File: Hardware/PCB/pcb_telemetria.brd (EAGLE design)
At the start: 77.5 x 104.1 mm, 33 parts

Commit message: update
adicao de rotas na pcb
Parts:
- moved SHUNTS 48.0 mm to (43.9, 3.87), turned to 0 degrees
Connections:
- net 25: no longer C_BAUX.2
- net 33: now also C_BAUX.2
- net C5: now also R20.1
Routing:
- net C5: track 0.00 -> 69.9 mm
- net C4: track 0.00 -> 69.6 mm
- net C7: track 0.49 -> 69.1 mm
- net C6: track 0.00 -> 68.3 mm
- net 2: track 9.94 -> 74.4 mm
- net 13: track 0.00 -> 46.1 mm
- net 33: track 0.00 -> 43.3 mm
- net C3: track 9.94 -> 32.6 mm
- net C2: track 24.6 -> 31.8 mm
- net C1: track 24.4 -> 30.9 mm
- net C0: track 25.3 -> 29.3 mm

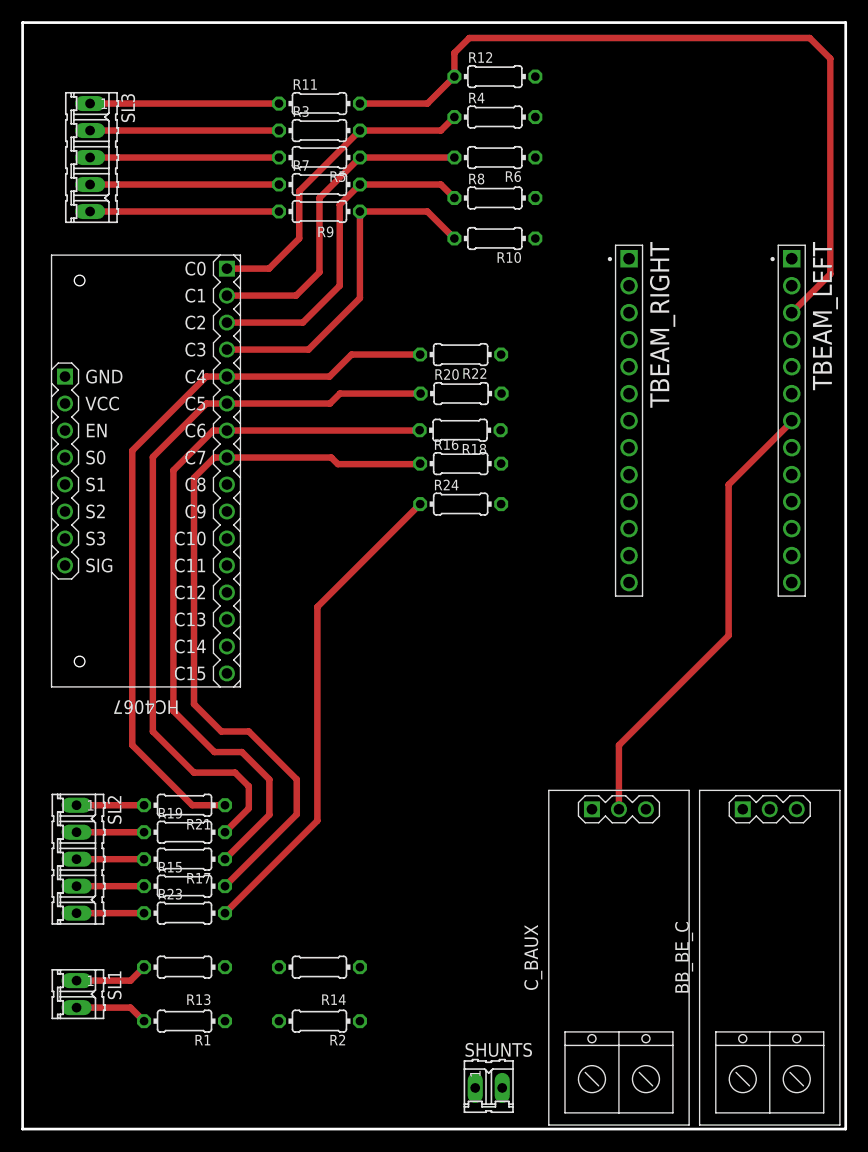
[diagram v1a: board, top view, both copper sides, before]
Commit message: Adicao de Rotas e mudanca de nomes
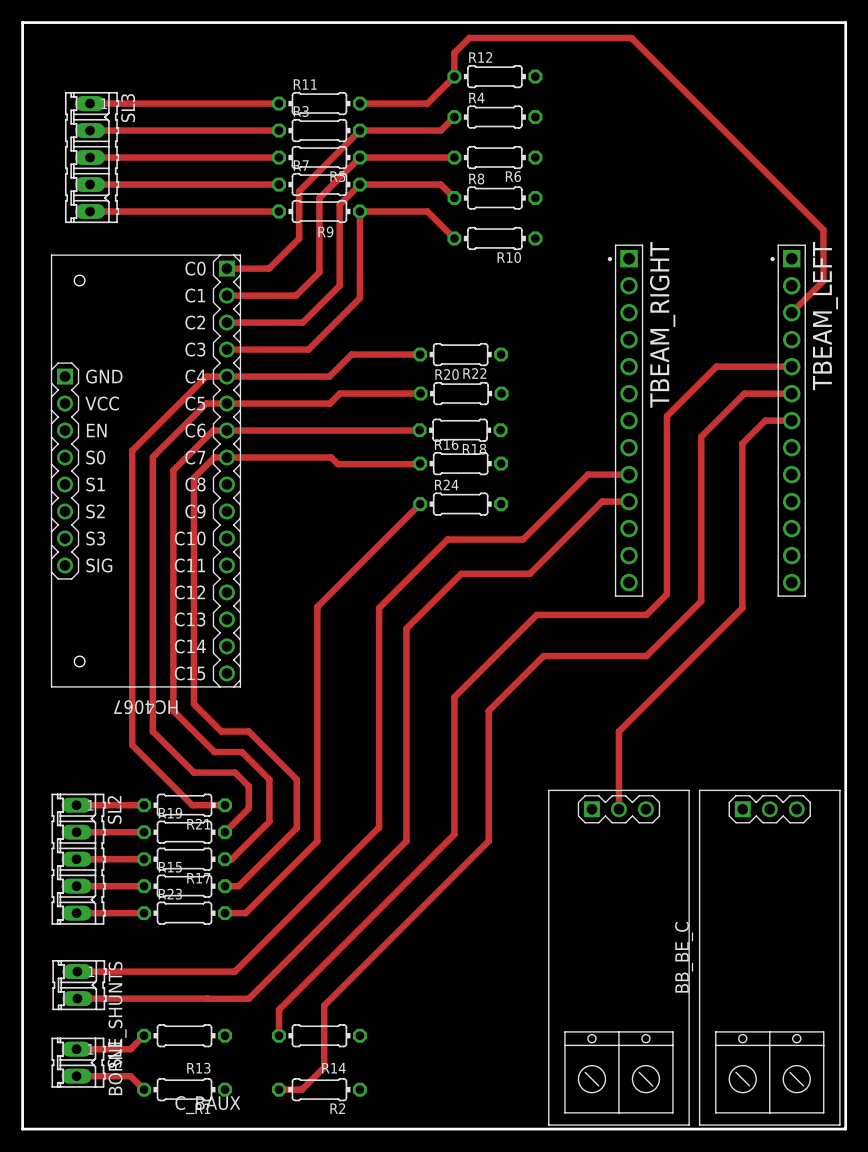
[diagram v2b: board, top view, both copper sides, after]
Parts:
- removed SHUNTS: (no value), con-amp-quick:02P
- added BORNE_SHUNTS: (no value), con-amp-quick:02P
- moved R13 6.45 mm to (15.2, 8.79)
- moved R14 6.45 mm to (27.9, 8.79)
- moved R1 6.45 mm to (15.2, 3.71)
- moved R2 6.45 mm to (27.9, 3.71)
- moved SL1 6.45 mm to (5.08, 6.25)
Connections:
- net 21: now also BORNE_SHUNTS.2; no longer SHUNTS.2
- net 22: now also BORNE_SHUNTS.1; no longer SHUNTS.1
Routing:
- net 25: track 0.00 -> 95.0 mm
- net 14: track 0.00 -> 93.2 mm
- net 22: track 0.00 -> 83.4 mm
- net 21: track 0.00 -> 83.0 mm
- net 2: track 74.4 -> 64.0 mm
- net 33: track 43.3 -> 44.8 mm
- net 13: track 46.1 -> 47.2 mm
- net C7: track 69.1 -> 69.9 mm

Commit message: ultima ligacao nao GND
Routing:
- net 13: track 47.2 -> 107.8 mm
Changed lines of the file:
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@@
 <wire x1="27.74188125" y1="49.14391875" x2="37.41928125" y2="58.82131875" width="0.6096" layer="1"/>
 <wire x1="27.74188125" y1="27.0764" x2="27.74188125" y2="49.14391875" width="0.6096" layer="1"/>
-<wire x1="37.41928125" y1="58.82131875" x2="72.39" y2="74.295" width="0" layer="19" extent="1-1"/>
+<wire x1="37.41928125" y1="58.82131875" x2="39.243" y2="58.82131875" width="0.6096" layer="1"/>
+<wire x1="39.243" y1="58.82131875" x2="39.354759375" y2="58.709559375" width="0.6096" layer="1"/>
+<wire x1="42.580559375" y1="61.935359375" x2="42.580559375" y2="73.548240625" width="0.6096" layer="1"/>
+<wire x1="42.580559375" y1="73.548240625" x2="54.8386" y2="85.80628125" width="0.6096" layer="1"/>
+<wire x1="39.354759375" y1="58.709559375" x2="42.580559375" y2="61.935359375" width="0.6096" layer="1"/>
+<wire x1="62.58051875" y1="78.709521875" x2="67.096640625" y2="74.1934" width="0.6096" layer="1"/>
+<wire x1="72.39" y1="74.295" x2="72.2884" y2="74.1934" width="0.6096" layer="1"/>
+<wire x1="72.2884" y1="74.1934" x2="67.096640625" y2="74.1934" width="0.6096" layer="1"/>
+<wire x1="54.8386" y1="85.80628125" x2="59.99988125" y2="85.80628125" width="0.6096" layer="1"/>
+<wire x1="59.99988125" y1="85.80628125" x2="62.58051875" y2="83.22564375" width="0.6096" layer="1"/>
+<wire x1="62.58051875" y1="83.22564375" x2="62.58051875" y2="78.709521875" width="0.6096" layer="1"/>
 </signal>
 <signal name="GND">
@@
 <wire x1="16.129" y1="61.2902" x2="18.044159375" y2="63.205359375" width="0.6096" layer="1"/>
 <wire x1="18.044159375" y1="63.205359375" x2="19.23288125" y2="63.205359375" width="0.6096" layer="1"/>
-<wire x1="19.23288125" y1="63.205359375" x2="29.05251875" y2="63.205359375" width="0.6096" layer="1"/>
-<wire x1="29.05251875" y1="63.205359375" x2="29.677359375" y2="62.58051875" width="0.6096" layer="1"/>
-<wire x1="29.677359375" y1="62.58051875" x2="37.36848125" y2="62.58051875" width="0.6096" layer="1"/>
+<wire x1="19.23288125" y1="63.205359375" x2="27.762203125" y2="63.205359375" width="0.6096" layer="1"/>
+<wire x1="27.762203125" y1="63.205359375" x2="28.38704375" y2="62.58051875" width="0.6096" layer="1"/>
+<wire x1="28.38704375" y1="62.58051875" x2="37.36848125" y2="62.58051875" width="0.6096" layer="1"/>
 <wire x1="37.36848125" y1="62.58051875" x2="37.41928125" y2="62.63131875" width="0.6096" layer="1"/>
 </signal>
